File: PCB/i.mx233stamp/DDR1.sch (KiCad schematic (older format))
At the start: 21 parts, among them U2 MT46V32M16TG, U3 M25P32

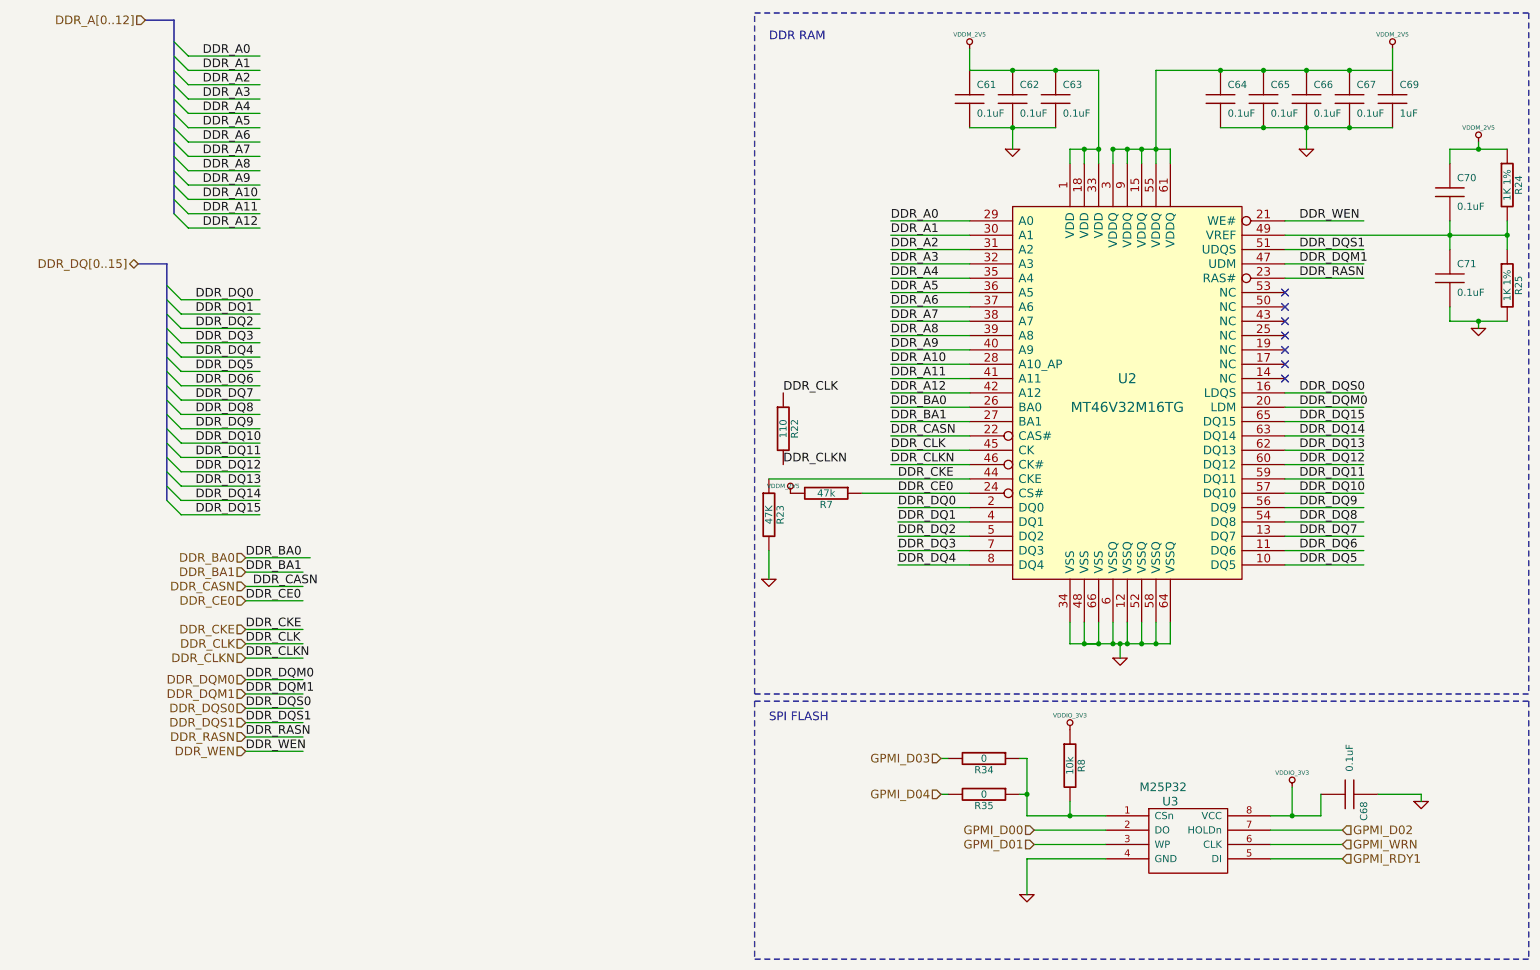
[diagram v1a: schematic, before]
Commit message: Adición del footprint del m25pxx, y re-organización del layout de la placa
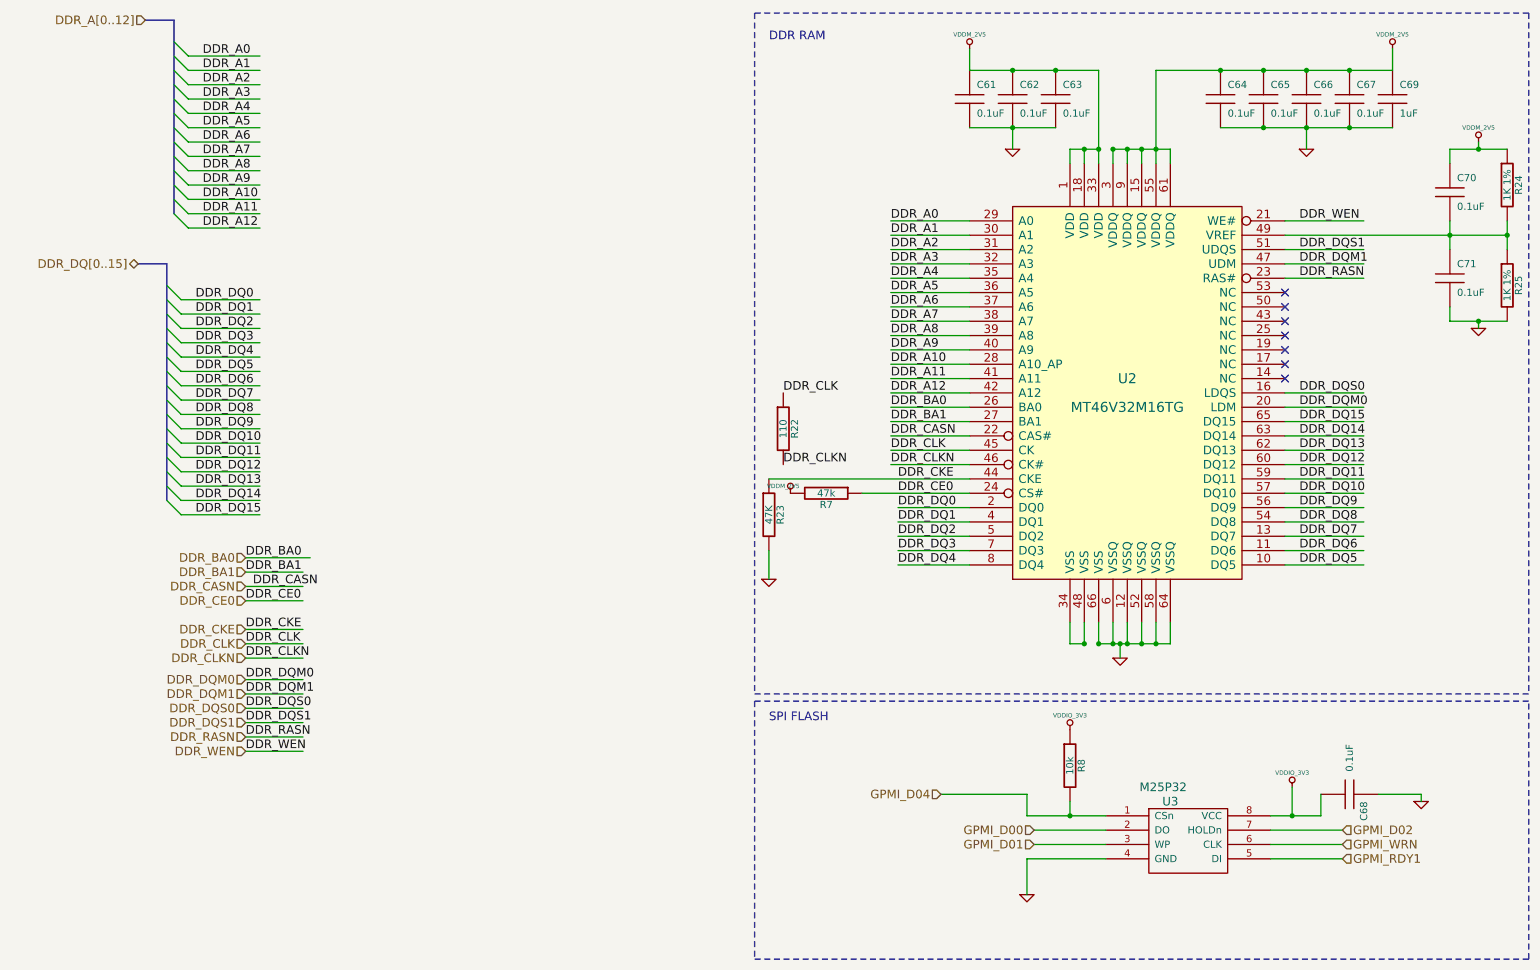
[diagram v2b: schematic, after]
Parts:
- removed R34, R35: 0, symbol R
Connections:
- net labels removed: GPMI_D03
- wire segments 142 -> 139
